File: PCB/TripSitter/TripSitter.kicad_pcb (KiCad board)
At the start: 6 copper layers, 268.6 x 82.9 mm, 257 parts, among them IC1 MT25QL256ABA1EW9-0SIT, IC2 MT41J128M16JT-125_K, IC701 IP4220CZ6, J1 Conn_ARM_JTAG_SWD_20, J10 EFM32_PinHeader_PortE, J11 EFM32_PinHeader_PortE, J12 EFM32_PinHeader_PortE, J13 EFM32_PinHeader_PortE, J14 Conn_02x10_Counter_Clockwise, J2 DE15_Plug_HighDensity_Mountin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, J201 Conn_ARM_JTAG_SWD_20, J3 USB_B_Micro, J4 USB_B_Micro, J5 Jack-DC, J6 EFM32_PinHeader_PortE, J7 HDMI_A_1.4, J801 Conn_02x05_Odd_Even, J802 Jack-DC, J803 USB_B_Micro, SW1 SW_Push_Open, SW2 SW_DPDT_x2, SW3 SW_DIP_x05, SW801 SW_DPDT_x2, U1 XC7A100T-FGG484, U2 TPS54325_PWP_14, U201 EFM32GG11B420F2048GQ100, U202 IS62WVS2568FBLL-20NLI, U5 TPS54294PWP, U6 IS62WVS2568FBLL-20NLI, U7 TPD12S520DBT, X1 XO53 100Mhz, Y201 48MHz

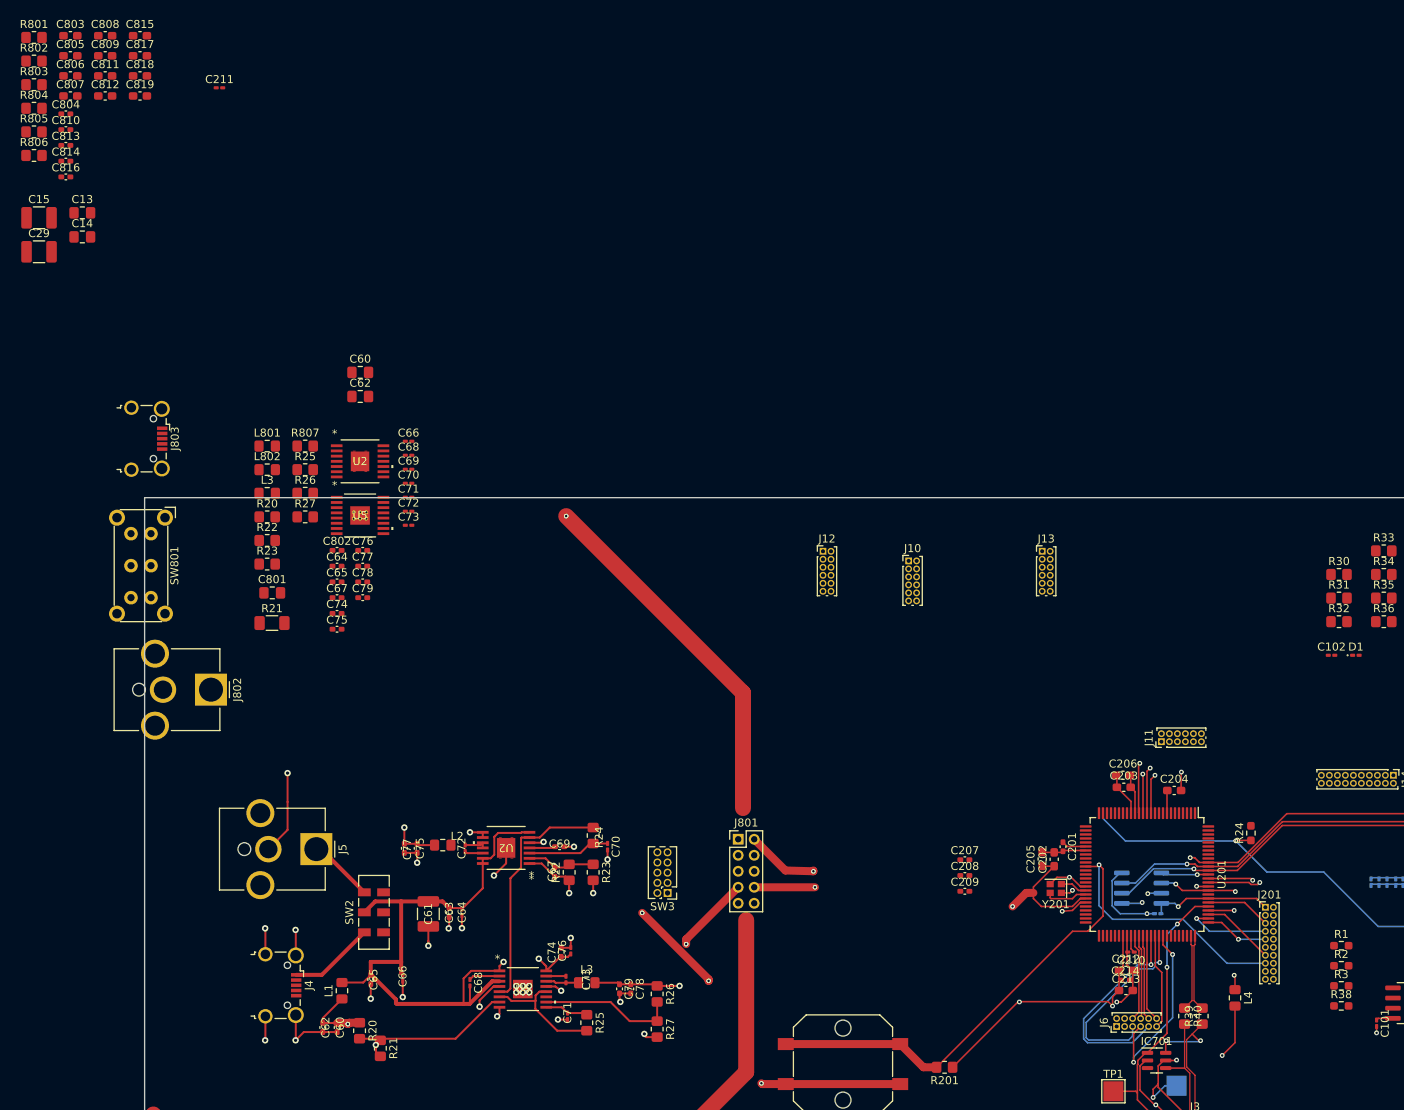
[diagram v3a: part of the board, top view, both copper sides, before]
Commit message: redo power circuit and add heat sink
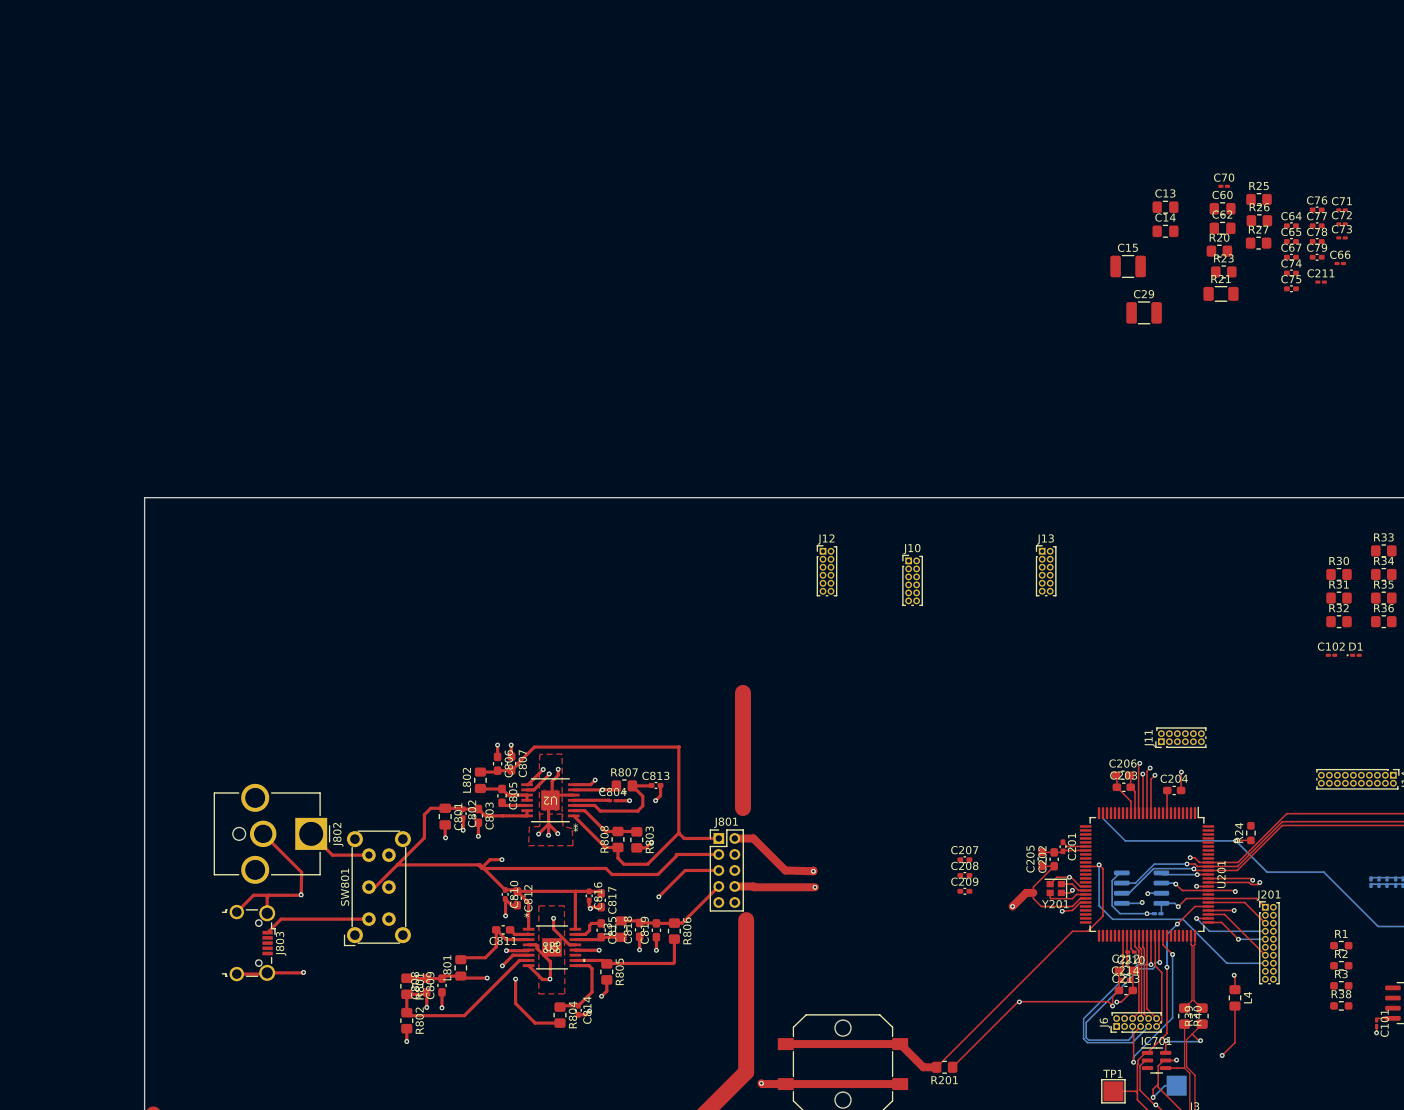
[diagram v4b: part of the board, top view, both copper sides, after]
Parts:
- removed the C60 at (39.8, 124.7)
- removed C61: 100uF, Capacitor_SMD:C_1210_3225Metric_Pad1.33x2.70mm_HandSolder
- removed the C62 at (38.0, 124.7)
- removed C63: 10uF, Capacitor_SMD:C_0402_1005Metric_Pad0.74x0.62mm_HandSolder
- removed the C64 at (55.4, 110.3)
- removed the C65 at (44.0, 118.7)
- removed the C66 at (48.0, 118.5)
- removed the C67 at (67.0, 105.3)
- removed C68: 100n, Capacitor_SMD:C_0201_0603Metric_Pad0.64x0.40mm_HandSolder
- removed C68: 100nF, Capacitor_SMD:C_0201_0603Metric_Pad0.64x0.40mm_HandSolder
- removed C69: 3.3nF, Capacitor_SMD:C_0402_1005Metric_Pad0.74x0.62mm_HandSolder
- removed the C70 at (73.6, 102.1)
- removed the C71 at (68.6, 123.3)
- removed the C72 at (55.8, 102.3)
- removed the C73 at (68.4, 118.7)
- removed the C74 at (67.8, 115.3)
- removed the C75 at (49.8, 102.3)
- removed the C76 at (69.0, 115.1)
- removed the C77 at (48.2, 102.3)
- removed the C78 at (76.5, 119.9)
- removed the C79 at (75.1, 119.9)
- removed the C804 at (5.86, 10.5)
- removed J4: USB_B_Micro, Connector_USB:USB_Micro-B_Wuerth_629105150521_CircularHoles
- removed J5: Jack-DC, Connector_BarrelJack:BarrelJack_CUI_PJ-063AH_Horizontal_CircularHoles
- removed L1, L2: 1.5uH, Inductor_SMD:L_0805_2012Metric_Pad1.15x1.40mm_HandSolder
- removed the L3 at (71.0, 119.1)
- removed the R20 at (42.6, 125.1)
- removed the R21 at (45.2, 127.3)
- removed R22: 21.3k, Resistor_SMD:R_0805_2012Metric_Pad1.20x1.40mm_HandSolder
- removed the R23 at (71.8, 105.3)
- removed the R24 at (71.8, 100.7)
- removed the R25 at (71.0, 124.1)
- removed the R26 at (79.8, 120.5)
- removed the R27 at (79.8, 124.9)
- removed SW2: SW_DPDT_x2, Button_Switch_SMD:SW_DPDT_CK_JS202011JCQN
- removed SW3: SW_DIP_x05, Connector_PinHeader_1.27mm:PinHeader_2x05_P1.27mm_Vertical
- removed the U2 at (60.9, 102.3)
- removed the U5 at (63.0, 119.9)
- R808: renamed from R22; value 21.3k -> 6.81k
- moved C211 139.8 mm to (162.8, 31.6)
- moved C29 138.3 mm to (140.6, 35.4)
- moved C15 136.3 mm to (138.6, 29.6)
- moved C13 135.4 mm to (143.3, 22.2)
- moved C14 135.4 mm to (143.3, 25.2)
- moved R804 131.0 mm to (67.6, 123.2), turned to -90 degrees
- moved R802 128.7 mm to (48.5, 123.9), turned to -90 degrees
- moved R801 127.4 mm to (48.5, 119.6), turned to -90 degrees
- moved R805 127.1 mm to (73.5, 117.8), turned to -90 degrees
- moved C76 126.7 mm to (162.3, 22.5)
- moved C64 126.7 mm to (159.1, 24.5)
- moved C65 126.7 mm to (159.1, 26.5)
- moved C67 126.7 mm to (159.1, 28.4)
- moved C74 126.7 mm to (159.1, 30.4)
- moved C75 126.7 mm to (159.1, 32.4)
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- renumbered C69 to C804
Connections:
- C811 pad 2: /PCB Power System/5V0 -> Net-(U5-SW1)
- J801 pad 10: +1V5 -> unconnected-(J801-Pin_10-Pad10)
- J801 pad 9: /PCB Power System/1V5 -> unconnected-(J801-Pin_9-Pad9)
- L801 pad 2: /PCB Power System/5V0 -> Net-(U5-SW1)
- R801 pad 2: GND -> Net-(U5-VFB1)
- R802 pad 1: GND -> Net-(U5-VFB1)
- R808 pad 1: /PCB Power System/1V5 -> /PCB Power System/1V0
- U2 pad 1: /PCB Power System/1V5 -> /PCB Power System/1V0
- U5 pad 3: /PCB Power System/5V0 -> Net-(U5-SW1)
- U5 pad 7: GND -> Net-(U5-VFB1)
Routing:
- net unconnected-(J801-Pin_10-Pad10): track 0.00 -> 137.0 mm
- net +1V5: track 163.1 -> 29.0 mm
- net /PCB Power System/1V5: track 50.1 -> 0.00 mm, vias 1 -> 0
- net /PCB Power System/1V8: track 96.3 -> 49.1 mm, vias 3 -> 2
- net /PCB Power System/1V0: track 95.8 -> 60.3 mm, vias 1 -> 0
- net /PCB Power System/3V3: track 40.1 -> 14.2 mm, vias 2 -> 0
- net GND: track 539.0 -> 518.4 mm, vias 76 -> 77
- net (no net): track 19.1 -> 0.14 mm
- net Net-(U5-EN2): track 15.5 -> 33.7 mm, vias 0 -> 3
- net Net-(U5-VFB1): track 0.00 -> 17.7 mm
- net VBUS: track 29.3 -> 42.7 mm
- net Net-(U5-SW1): track 0.00 -> 11.8 mm
- net Net-(U2-PG): track 31.2 -> 40.3 mm, vias 0 -> 2
- net Net-(SW801A-C): track 0.00 -> 8.32 mm
- net Net-(U5-VREG5): track 5.45 -> 9.95 mm
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- added copper zone on F.Cu, net GND

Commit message: pcb: Finalized routing without DDR3
Added ground and power plane, layed out all the components, fanned out
BGA. QSPI between FPGA->MCU->SRAM and MCU->SRAM is routed. Most is done
but DRC does not pass so do not produce.
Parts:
- removed C106, C107, C108, C109, C110, C111, C12, C20, C21: 4.7uF, Capacitor_SMD:C_0201_0603Metric_Pad0.64x0.40mm_HandSolder
- removed C11, C112, C113, C17, C18, C2, C22, C23, C24, C3, C4, C5, C6, C7, C8: 470nF, Capacitor_SMD:C_0201_0603Metric_Pad0.64x0.40mm_HandSolder
- removed C16, C96: 100uF, Capacitor_SMD:C_0805_2012Metric_Pad1.18x1.45mm_HandSolder
- removed C19: 47uF, Capacitor_SMD:C_0603_1608Metric_Pad1.08x0.95mm_HandSolder
- removed C207, C208: 10nF, Capacitor_SMD:C_0402_1005Metric_Pad0.74x0.62mm_HandSolder
- removed C209, C65, C67, C74: 10uF, Capacitor_SMD:C_0402_1005Metric_Pad0.74x0.62mm_HandSolder
- removed the C25 at (229.6, 125.9)
- removed the C25 at (199.6, 117.1)
- removed the C46 at (204.0, 127.8)
- removed the C46 at (204.4, 114.2)
- removed the C47 at (204.0, 128.8)
- removed the C47 at (199.4, 111.9)
- removed the C49 at (203.9, 132.1)
- removed the C49 at (209.4, 113.5)
- removed C59, C70, C71: 1uF, Capacitor_SMD:C_0201_0603Metric_Pad0.64x0.40mm_HandSolder
- removed C60, C62: 22uF, Capacitor_SMD:C_0805_2012Metric_Pad1.18x1.45mm_HandSolder
- removed C64: 0.1uF, Capacitor_SMD:C_0402_1005Metric_Pad0.74x0.62mm_HandSolder
- removed C66, C72, C73: 100nF, Capacitor_SMD:C_0201_0603Metric_Pad0.64x0.40mm_HandSolder
- removed C75, C77: 22uF, Capacitor_SMD:C_0402_1005Metric_Pad0.74x0.62mm_HandSolder
- removed C76: 100nF, Capacitor_SMD:C_0402_1005Metric_Pad0.74x0.62mm_HandSolder
- removed C78, C79: 22u, Capacitor_SMD:C_0402_1005Metric_Pad0.74x0.62mm_HandSolder
- removed C87: 47uF, Capacitor_SMD:C_1210_3225Metric_Pad1.33x2.70mm_HandSolder
- removed C88, C89: 4.7uF, Capacitor_SMD:C_0805_2012Metric_Pad1.18x1.45mm_HandSolder
- removed C94, C95: 0.1uF, Capacitor_SMD:C_0201_0603Metric_Pad0.64x0.40mm_HandSolder
- removed IC2: MT41J128M16JT-125_K, Package_BGA:Micron_FBGA-96_8x14mm_Layout9x16_P0.8mm
- removed J10, J11, J12, J13: EFM32_PinHeader_PortE, Connector_PinHeader_1.00mm:PinHeader_2x06_P1.00mm_Vertical
- removed J14: Conn_02x10_Counter_Clockwise, Connector_PinHeader_1.00mm:PinHeader_2x10_P1.00mm_Vertical
- removed R19: 100R, Resistor_SMD:R_0201_0603Metric_Pad0.64x0.40mm_HandSolder
- removed the R20 at (150.1, 27.7)
- removed the R20 at (190.3, 123.7)
- removed the R21 at (150.2, 33.0)
- removed the R21 at (191.5, 126.1)
- removed the R23 at (150.6, 30.3)
- removed the R23 at (215.8, 100.9)
- removed R25: 100k, Resistor_SMD:R_0805_2012Metric_Pad1.20x1.40mm_HandSolder
- removed R26: 73.2k, Resistor_SMD:R_0805_2012Metric_Pad1.20x1.40mm_HandSolder
- removed R27: 22.1k, Resistor_SMD:R_0805_2012Metric_Pad1.20x1.40mm_HandSolder
- removed R28: 240, Resistor_SMD:R_0805_2012Metric_Pad1.20x1.40mm_HandSolder
- removed X1: XO53 100Mhz, Oscillator:Oscillator_SMD_EuroQuartz_XO53-4Pin_5.0x3.2mm_HandSoldering
- added C25: 470nF, Capacitor_SMD:C_0402_1005Metric_Pad0.74x0.62mm_HandSolder, B.Cu at (168.7, 56.0)
- added C46: 4.7uF, Capacitor_SMD:C_0201_0603Metric_Pad0.64x0.40mm_HandSolder, B.Cu at (158.8, 68.6)
- added C47: 4.7uF, Capacitor_SMD:C_0201_0603Metric_Pad0.64x0.40mm_HandSolder, B.Cu at (160.5, 68.5)
- added C49: 4.7uF, Capacitor_SMD:C_0201_0603Metric_Pad0.64x0.40mm_HandSolder, B.Cu at (165.3, 65.9)
- added C50: 4.7uF, Capacitor_SMD:C_0201_0603Metric_Pad0.64x0.40mm_HandSolder, B.Cu at (162.6, 68.5)
- added C51: 470nF, Capacitor_SMD:C_0201_0603Metric_Pad0.64x0.40mm_HandSolder, B.Cu at (165.3, 67.6)
- added C54: 470nF, Capacitor_SMD:C_0201_0603Metric_Pad0.64x0.40mm_HandSolder, B.Cu at (169.1, 59.9)
- added C55: 470nF, Capacitor_SMD:C_0201_0603Metric_Pad0.64x0.40mm_HandSolder, B.Cu at (170.9, 62.5)
- added C56: 470nF, Capacitor_SMD:C_0201_0603Metric_Pad0.64x0.40mm_HandSolder, B.Cu at (169.7, 61.2)
- added C58: 470nF, Capacitor_SMD:C_0201_0603Metric_Pad0.64x0.40mm_HandSolder, B.Cu at (168.0, 63.9)
- added C69: 3.3nF, Capacitor_SMD:C_0201_0603Metric_Pad0.64x0.40mm_HandSolder, F.Cu at (58.5, 49.5)
- added C813: 1uF, Capacitor_SMD:C_0402_1005Metric_Pad0.74x0.62mm_HandSolder, F.Cu at (74.9, 51.7)
- added C816: 10uF, Capacitor_SMD:C_0402_1005Metric_Pad0.74x0.62mm_HandSolder, F.Cu at (52.3, 49.6)
- added L801: 1.5uH, Inductor_SMD:L_0805_2012Metric_Pad1.15x1.40mm_HandSolder, F.Cu at (80.9, 58.2)
- added R20: 10k, Resistor_SMD:R_0805_2012Metric_Pad1.20x1.40mm_HandSolder, F.Cu at (193.4, 52.6)
- added R21: 10k, Resistor_SMD:R_0805_2012Metric_Pad1.20x1.40mm_HandSolder, F.Cu at (193.4, 59.7)
- added R22: 21.3k, Resistor_SMD:R_0805_2012Metric_Pad1.20x1.40mm_HandSolder, F.Cu at (69.4, 54.3)
- added R23: 4.7k, Resistor_SMD:R_0603_1608Metric_Pad0.98x0.95mm_HandSolder, F.Cu at (187.4, 61.3)
- added U4: DSC1001DL5-100.0000T, Footprints:CDFN4_2P5X2_MCH-L, F.Cu at (189.0, 50.7)
- C1: value 330uF -> 0.1uF; footprint Capacitor_Tantalum_SMD:CP_EIA-7343-43_Kemet-X_Pad2.25x2.55mm_HandSolder -> Capacitor_SMD:C_0603_1608Metric_Pad1.08x0.95mm_HandSolder; moved to F.Cu
- C101, C102, C103, C214, C36, C37, C38, C98, D1, IC1, R1, R35, R36, R37, R38: moved to B.Cu
- C104, TP4: moved to F.Cu
- C13, C14, C26, C27: value 4.7uF -> 470nF; footprint Capacitor_SMD:C_0805_2012Metric_Pad1.18x1.45mm_HandSolder -> Capacitor_SMD:C_0402_1005Metric_Pad0.74x0.62mm_HandSolder; moved to B.Cu
- C15: value 47uF -> 470nF; footprint Capacitor_SMD:C_1210_3225Metric_Pad1.33x2.70mm_HandSolder -> Capacitor_SMD:C_0402_1005Metric_Pad0.74x0.62mm_HandSolder; moved to B.Cu
- C202, C203, C205: footprint Capacitor_SMD:C_0603_1608Metric_Pad1.08x0.95mm_HandSolder -> Capacitor_SMD:C_0402_1005Metric_Pad0.74x0.62mm_HandSolder
- C204, C206, C212, C213: footprint Capacitor_SMD:C_0603_1608Metric_Pad1.08x0.95mm_HandSolder -> Capacitor_SMD:C_0402_1005Metric_Pad0.74x0.62mm_HandSolder; moved to B.Cu
- C210: footprint Capacitor_SMD:C_0201_0603Metric_Pad0.64x0.40mm_HandSolder -> Capacitor_SMD:C_0402_1005Metric_Pad0.74x0.62mm_HandSolder; moved to B.Cu
- C28, C31: value 470nF -> 4.7uF; footprint Capacitor_SMD:C_0201_0603Metric_Pad0.64x0.40mm_HandSolder -> Capacitor_SMD:C_0402_1005Metric_Pad0.74x0.62mm_HandSolder
- C29: value 100uF -> 4.7uF; footprint Capacitor_SMD:C_1210_3225Metric_Pad1.33x2.70mm_HandSolder -> Capacitor_SMD:C_0402_1005Metric_Pad0.74x0.62mm_HandSolder; moved to B.Cu
- C30: footprint Capacitor_SMD:C_0201_0603Metric_Pad0.64x0.40mm_HandSolder -> Capacitor_SMD:C_0402_1005Metric_Pad0.74x0.62mm_HandSolder
- C32: value 470nF -> 47uF; footprint Capacitor_SMD:C_0201_0603Metric_Pad0.64x0.40mm_HandSolder -> Capacitor_SMD:C_0603_1608Metric_Pad1.08x0.95mm_HandSolder
- C33: value 4.7uF -> 100uF
- C34: value 4.7uF -> 330uF; footprint Capacitor_SMD:C_0805_2012Metric_Pad1.18x1.45mm_HandSolder -> Capacitor_Tantalum_SMD:CP_EIA-7343-43_Kemet-X_Pad2.25x2.55mm_HandSolder; moved to B.Cu
- C35: value 47uF -> 4.7uF; footprint Capacitor_SMD:C_1210_3225Metric_Pad1.33x2.70mm_HandSolder -> Capacitor_SMD:C_0201_0603Metric_Pad0.64x0.40mm_HandSolder; moved to B.Cu
- C48: value 470nF -> 4.7uF
- C52, C53, C57: value 0.1uF -> 470nF; moved to B.Cu
- C804: value 3.3nF -> 10uF; footprint Capacitor_SMD:C_0201_0603Metric_Pad0.64x0.40mm_HandSolder -> Capacitor_SMD:C_0402_1005Metric_Pad0.74x0.62mm_HandSolder
- J1: footprint Connector_PinHeader_1.00mm:PinHeader_2x10_P1.00mm_Vertical -> Connector_PinHeader_2.54mm:PinHeader_2x07_P2.54mm_Vertical_SMD
- J201: footprint Connector_PinHeader_1.00mm:PinHeader_2x10_P1.00mm_Vertical -> Connector_PinHeader_1.27mm:PinHeader_2x10_P1.27mm_Vertical_SMD
- R30: footprint Resistor_SMD:R_0805_2012Metric_Pad1.20x1.40mm_HandSolder -> Resistor_SMD:R_0603_1608Metric_Pad0.98x0.95mm_HandSolder
- R31, R32: footprint Resistor_SMD:R_0805_2012Metric_Pad1.20x1.40mm_HandSolder -> Resistor_SMD:R_0603_1608Metric_Pad0.98x0.95mm_HandSolder; moved to B.Cu
- SW1: footprint Button_Switch_SMD:SW_Push_1P1T_NO_CK_PTS125Sx43PSMTR -> Button_Switch_SMD:SW_Push_SPST_NO_Alps_SKRK
- SW801: footprint Button_Switch_THT:SW_E-Switch_EG2219_DPDT_Angled -> Button_Switch_THT:SW_E-Switch_EG1224_SPDT_Angled
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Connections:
- C1 pad 2: +1V0 -> +3.3V
- C13 pad 1: +1V5 -> +1V8
- C14 pad 1: +1V5 -> +1V8
- C15 pad 1: +1V5 -> +1V8
- C26 pad 1: +1V5 -> +1V8
- C27 pad 1: +1V5 -> +1V0
- C28 pad 1: +3.3V -> +1V8
- C29 pad 1: +1V5 -> +1V8
- C30 pad 1: +3.3V -> +1V0
- C31 pad 1: +3.3V -> +1V8
- C32 pad 1: +3.3V -> +1V8
- C33 pad 1: +3.3V -> +1V0
- C34 pad 1: +3.3V -> GND
- C34 pad 2: GND -> +1V0
- C35 pad 1: +3.3V -> +1V0
- C48 pad 1: +1V5 -> +1V0
- C52 pad 1: +3.3V -> +1V0
- C53 pad 1: +3.3V -> +1V0
- C57 pad 1: GND -> +1V0
- C57 pad 2: +3.3V -> GND
- C804 pad 1: Net-(U2-SS) -> /PCB Power System/1V5
- C804 pad 2: GND -> Net-(U2-VFB)
- C811 pad 2: Net-(U5-SW1) -> /PCB Power System/5V0
- IC701 pad 5: VBUS -> +5V
- J3 pad 1: VBUS -> +5V
- J3 pad 5: GND -> unconnected-(J3-GND-Pad5)
- J6 pad 1: /MCU EFM32GG11B420/MCU_EXTIO_PC6 -> unconnected-(J6-Pin_1-Pad1)
- J6 pad 11: /MCU EFM32GG11B420/PE_5 -> /MCU EFM32GG11B420/PE_4
- J6 pad 2: /MCU EFM32GG11B420/MCU_EXTIO_PC4 -> unconnected-(J6-Pin_2-Pad2)
- J6 pad 3: /MCU EFM32GG11B420/MCU_EXTIO_PC7 -> unconnected-(J6-Pin_3-Pad3)
- J6 pad 4: /MCU EFM32GG11B420/MCU_EXTIO_PC5 -> unconnected-(J6-Pin_4-Pad4)
- J6 pad 5: /MCU EFM32GG11B420/PE_6 -> /MCU EFM32GG11B420/PE_7
- J6 pad 7: /MCU EFM32GG11B420/PE_7 -> /MCU EFM32GG11B420/PE_6
- J6 pad 9: /MCU EFM32GG11B420/PE_4 -> /MCU EFM32GG11B420/PE_5
- J801 pad 10: unconnected-(J801-Pin_10-Pad10) -> +1V5
- J801 pad 9: unconnected-(J801-Pin_9-Pad9) -> /PCB Power System/1V5
- J802 pad 1: Net-(SW801A-C) -> Net-(SW801A-A)
- J803 pad 1: VBUS -> +5V
- L4 pad 2: VBUS -> +5V
- R24 pad 2: +3V3 -> +3.3V
- R801 pad 2: Net-(U5-VFB1) -> GND
- R802 pad 1: Net-(U5-VFB1) -> GND
- SW801 pad 1: VBUS -> Net-(SW801A-A)
- SW801 pad 3: Net-(SW801A-C) -> +5V
- TP4 pad 1: VBUS -> +5V
- U1 pad A1: (no net) -> unconnected-(U1C-IO_L1N_T0_AD4N_35-PadA1)
- U1 pad A13: unconnected-(U1B-IO_L10P_T1_16-PadA13) -> MCU_PE7
- U1 pad A14: unconnected-(U1B-IO_L10N_T1_16-PadA14) -> MCU_PE8
- U1 pad AA1: /FPGA Artix-7 100T 1FGG484C/DDR3/DDR3_DQ0 -> unconnected-(U1H-IO_L7P_T1_34-PadAA1)
- U1 pad AA10: Net-(J14-Pin_7) -> unconnected-(U1A-IO_L9P_T1_DQS_13-PadAA10)
- U1 pad AA11: Net-(J14-Pin_8) -> unconnected-(U1A-IO_L9N_T1_DQS_13-PadAA11)
- U1 pad AA17: +3.3V -> unconnected-(U1A-VCCO_13-PadAA17)
- U1 pad AA18: unconnected-(U1A-IO_L17P_T2_A14_D30_14-PadAA18) -> /FPGA Artix-7 100T 1FGG484C/VGA_B2
- U1 pad AA19: unconnected-(U1A-IO_L15P_T2_DQS_RDWR_B_14-PadAA19) -> /FPGA Artix-7 100T 1FGG484C/VGA_B1
- U1 pad AA20: /FPGA Artix-7 100T 1FGG484C/VGA_B2 -> /FPGA Artix-7 100T 1FGG484C/VGA_G3
- U1 pad AA21: /FPGA Artix-7 100T 1FGG484C/VGA_G0 -> /FPGA Artix-7 100T 1FGG484C/VGA_G1
- U1 pad AA3: /FPGA Artix-7 100T 1FGG484C/DDR3/DDR3_A8 -> unconnected-(U1H-IO_L9N_T1_DQS_34-PadAA3)
- U1 pad AA4: /FPGA Artix-7 100T 1FGG484C/DDR3/DDR3_BA2 -> unconnected-(U1H-IO_L11N_T1_SRCC_34-PadAA4)
- U1 pad AA5: /FPGA Artix-7 100T 1FGG484C/DDR3/DDR3_DQ6 -> unconnected-(U1H-IO_L10P_T1_34-PadAA5)
- U1 pad AA6: /FPGA Artix-7 100T 1FGG484C/DDR3/DDR3_A12 -> unconnected-(U1H-IO_L18N_T2_34-PadAA6)
- U1 pad AA7: +1V5 -> unconnected-(U1H-VCCO_34-PadAA7)
- U1 pad AA8: /FPGA Artix-7 100T 1FGG484C/DDR3/DDR3_UDQS_P -> unconnected-(U1H-IO_L22P_T3_34-PadAA8)
- U1 pad AA9: Net-(J14-Pin_5) -> unconnected-(U1A-IO_L8P_T1_13-PadAA9)
- U1 pad AB1: /FPGA Artix-7 100T 1FGG484C/DDR3/DDR3_LDQS_P -> unconnected-(U1H-IO_L7N_T1_34-PadAB1)
- U1 pad AB10: Net-(J14-Pin_6) -> unconnected-(U1A-IO_L8N_T1_13-PadAB10)
- U1 pad AB11: Net-(J14-Pin_3) -> unconnected-(U1A-IO_L7P_T1_13-PadAB11)
- U1 pad AB12: Net-(J14-Pin_4) -> unconnected-(U1A-IO_L7N_T1_13-PadAB12)
- U1 pad AB14: +3.3V -> unconnected-(U1A-VCCO_13-PadAB14)
- U1 pad AB18: unconnected-(U1A-IO_L17N_T2_A13_D29_14-PadAB18) -> /FPGA Artix-7 100T 1FGG484C/VGA_B3
- U1 pad AB2: /FPGA Artix-7 100T 1FGG484C/DDR3/DDR3_LDQS_N -> unconnected-(U1H-IO_L8N_T1_34-PadAB2)
- U1 pad AB20: /FPGA Artix-7 100T 1FGG484C/VGA_B3 -> /FPGA Artix-7 100T 1FGG484C/VGA_B0
- U1 pad AB21: /FPGA Artix-7 100T 1FGG484C/VGA_B1 -> /FPGA Artix-7 100T 1FGG484C/VGA_G2
- U1 pad AB22: /FPGA Artix-7 100T 1FGG484C/VGA_B0 -> /FPGA Artix-7 100T 1FGG484C/VGA_G0
- U1 pad AB3: /FPGA Artix-7 100T 1FGG484C/DDR3/DDR3_DQ4 -> unconnected-(U1H-IO_L8P_T1_34-PadAB3)
- U1 pad AB4: +1V5 -> unconnected-(U1H-VCCO_34-PadAB4)
- U1 pad AB5: /FPGA Artix-7 100T 1FGG484C/DDR3/DDR3_DQ1 -> unconnected-(U1H-IO_L10N_T1_34-PadAB5)
- U1 pad AB6: /FPGA Artix-7 100T 1FGG484C/DDR3/DDR3_LDM -> unconnected-(U1H-IO_L20N_T3_34-PadAB6)
- U1 pad AB7: /FPGA Artix-7 100T 1FGG484C/DDR3/DDR3_DQ8 -> unconnected-(U1H-IO_L20P_T3_34-PadAB7)
- U1 pad AB8: /FPGA Artix-7 100T 1FGG484C/DDR3/DDR3_DQ12 -> unconnected-(U1H-IO_L22N_T3_34-PadAB8)
- U1 pad B1: (no net) -> unconnected-(U1C-IO_L1P_T0_AD4P_35-PadB1)
- U1 pad B2: (no net) -> unconnected-(U1C-IO_L2N_T0_AD12N_35-PadB2)
- U1 pad C1: (no net) -> unconnected-(U1C-VCCO_35-PadC1)
- U1 pad C15: unconnected-(U1B-IO_L3N_T0_DQS_16-PadC15) -> MCU_PE8
- U1 pad C19: unconnected-(U1B-IO_L13N_T2_MRCC_16-PadC19) -> /FPGA Artix-7 100T 1FGG484C/SRAM_QSPI0_CS0
- U1 pad C2: (no net) -> unconnected-(U1C-IO_L2P_T0_AD12P_35-PadC2)
- U1 pad D1: (no net) -> unconnected-(U1C-IO_L3N_T0_DQS_AD5N_35-PadD1)
- U1 pad D14: /MCU EFM32GG11B420/QSPI0_SCLK -> /FPGA Artix-7 100T 1FGG484C/SRAM_QSPI0_SCLK
- U1 pad D2: (no net) -> unconnected-(U1C-IO_L4N_T0_35-PadD2)
- U1 pad E1: (no net) -> unconnected-(U1C-IO_L3P_T0_DQS_AD5P_35-PadE1)
- U1 pad E12: +1V0 -> GND
- U1 pad E2: (no net) -> unconnected-(U1C-IO_L4P_T0_35-PadE2)
- U1 pad E3: (no net) -> unconnected-(U1C-IO_L6N_T0_VREF_35-PadE3)
- U1 pad F1: (no net) -> unconnected-(U1C-IO_L5N_T0_AD13N_35-PadF1)
- U1 pad F16: unconnected-(U1B-IO_L2P_T0_16-PadF16) -> MCU_PE9
- U1 pad F2: (no net) -> unconnected-(U1C-VCCO_35-PadF2)
- U1 pad F3: (no net) -> unconnected-(U1C-IO_L6P_T0_35-PadF3)
- U1 pad F4: (no net) -> unconnected-(U1C-IO_0_35-PadF4)
- U1 pad G1: (no net) -> unconnected-(U1C-IO_L5P_T0_AD13P_35-PadG1)
- U1 pad G2: (no net) -> unconnected-(U1C-IO_L8N_T1_AD14N_35-PadG2)
- U1 pad G21: HDMI_CLK_P -> HDMI_CLK_N
- U1 pad G22: HDMI_CLK_N -> HDMI_CLK_P
- U1 pad G3: (no net) -> unconnected-(U1C-IO_L11N_T1_SRCC_35-PadG3)
- U1 pad G4: (no net) -> unconnected-(U1C-IO_L12N_T1_MRCC_35-PadG4)
- U1 pad H10: +1V8 -> +1V0
- U1 pad H12: +1V0 -> +1V8
- U1 pad H2: (no net) -> unconnected-(U1C-IO_L8P_T1_AD14P_35-PadH2)
- U1 pad H3: (no net) -> unconnected-(U1C-IO_L11P_T1_SRCC_35-PadH3)
- U1 pad H4: (no net) -> unconnected-(U1C-IO_L12P_T1_MRCC_35-PadH4)
- U1 pad H5: (no net) -> unconnected-(U1C-IO_L10N_T1_AD15N_35-PadH5)
- U1 pad H6: (no net) -> unconnected-(U1C-VCCO_35-PadH6)
- U1 pad H8: +1V8 -> +1V0
- U1 pad J1: (no net) -> unconnected-(U1C-IO_L7N_T1_AD6N_35-PadJ1)
- U1 pad J2: (no net) -> unconnected-(U1C-IO_L9N_T1_DQS_AD7N_35-PadJ2)
- U1 pad J3: (no net) -> unconnected-(U1C-VCCO_35-PadJ3)
- U1 pad J4: (no net) -> unconnected-(U1C-IO_L13N_T2_MRCC_35-PadJ4)
- U1 pad J5: (no net) -> unconnected-(U1C-IO_L10P_T1_AD15P_35-PadJ5)
- U1 pad J6: (no net) -> unconnected-(U1C-IO_L17N_T2_35-PadJ6)
- U1 pad J7: +1V8 -> +1V0
- U1 pad J9: +1V8 -> +1V0
- U1 pad K1: (no net) -> unconnected-(U1C-IO_L7P_T1_AD6P_35-PadK1)
- U1 pad K10: +1V0 -> +1V8
- U1 pad K12: +1V0 -> +1V8
- U1 pad K2: (no net) -> unconnected-(U1C-IO_L9P_T1_DQS_AD7P_35-PadK2)
- U1 pad K3: (no net) -> unconnected-(U1C-IO_L14N_T2_SRCC_35-PadK3)
- U1 pad K4: (no net) -> unconnected-(U1C-IO_L13P_T2_MRCC_35-PadK4)
- U1 pad K6: (no net) -> unconnected-(U1C-IO_L17P_T2_35-PadK6)
- U1 pad K8: +1V8 -> +1V0
- U1 pad K9: +1V0 -> GND
- U1 pad L1: (no net) -> unconnected-(U1C-IO_L15N_T2_DQS_35-PadL1)
- U1 pad L3: (no net) -> unconnected-(U1C-IO_L14P_T2_SRCC_35-PadL3)
- U1 pad L4: (no net) -> unconnected-(U1C-IO_L18N_T2_35-PadL4)
- U1 pad L5: (no net) -> unconnected-(U1C-IO_L18P_T2_35-PadL5)
- U1 pad L6: (no net) -> unconnected-(U1C-IO_25_35-PadL6)
- U1 pad L7: +1V8 -> +1V0
- U1 pad L9: unconnected-(U1F-VREFN_0-PadL9) -> GND
- U1 pad M1: (no net) -> unconnected-(U1C-IO_L15P_T2_DQS_35-PadM1)
- U1 pad M10: unconnected-(U1F-VREFP_0-PadM10) -> GND
- U1 pad M12: +1V0 -> +1V8
- U1 pad M2: (no net) -> unconnected-(U1C-IO_L16N_T2_35-PadM2)
- U1 pad M3: (no net) -> unconnected-(U1C-IO_L16P_T2_35-PadM3)
- U1 pad M4: (no net) -> unconnected-(U1C-VCCO_35-PadM4)
- U1 pad M5: (no net) -> unconnected-(U1C-IO_L23N_T3_35-PadM5)
- U1 pad M6: (no net) -> unconnected-(U1C-IO_L23P_T3_35-PadM6)
- U1 pad M8: +1V8 -> +1V0
- U1 pad N1: (no net) -> unconnected-(U1C-VCCO_35-PadN1)
- U1 pad N2: (no net) -> unconnected-(U1C-IO_L22N_T3_35-PadN2)
- U1 pad N3: (no net) -> unconnected-(U1C-IO_L19N_T3_VREF_35-PadN3)
- U1 pad N4: (no net) -> unconnected-(U1C-IO_L19P_T3_35-PadN4)
- U1 pad N5: (no net) -> unconnected-(U1C-IO_L24N_T3_35-PadN5)
- U1 pad N7: +1V8 -> +1V0
- U1 pad P1: (no net) -> unconnected-(U1C-IO_L20N_T3_35-PadP1)
- U1 pad P12: +1V0 -> +1V8
- U1 pad P2: (no net) -> unconnected-(U1C-IO_L22P_T3_35-PadP2)
- U1 pad P4: (no net) -> unconnected-(U1C-IO_L21N_T3_DQS_35-PadP4)
- U1 pad P5: (no net) -> unconnected-(U1C-IO_L21P_T3_DQS_35-PadP5)
- U1 pad P6: (no net) -> unconnected-(U1C-IO_L24P_T3_35-PadP6)
- U1 pad P8: +1V8 -> +1V0
- U1 pad R1: (no net) -> unconnected-(U1C-IO_L20P_T3_35-PadR1)
- U1 pad R11: +1V0 -> +1V8
- U1 pad R2: /FPGA Artix-7 100T 1FGG484C/DDR3/DDR3_DQ2 -> unconnected-(U1H-IO_L3N_T0_DQS_34-PadR2)
- U1 pad R3: /FPGA Artix-7 100T 1FGG484C/DDR3/DDR3_DQ7 -> unconnected-(U1H-IO_L3P_T0_DQS_34-PadR3)
- U1 pad R4: /FPGA Artix-7 100T 1FGG484C/DDR3/DDR3_CKE -> unconnected-(U1H-IO_L13P_T2_MRCC_34-PadR4)
- U1 pad R5: +1V5 -> unconnected-(U1H-VCCO_34-PadR5)
- U1 pad R6: /FPGA Artix-7 100T 1FGG484C/DDR3/DDR3_A7 -> unconnected-(U1H-IO_L17P_T2_34-PadR6)
- U1 pad T1: /FPGA Artix-7 100T 1FGG484C/DDR3/DDR3_DQ11 -> unconnected-(U1H-IO_L1P_T0_34-PadT1)
- U1 pad T14: /FPGA Artix-7 100T 1FGG484C/FPGA_BANK13_20 -> unconnected-(U1A-IO_L15P_T2_DQS_13-PadT14)
- U1 pad T15: /FPGA Artix-7 100T 1FGG484C/FPGA_BANK13_21 -> unconnected-(U1A-IO_L15N_T2_DQS_13-PadT15)
- U1 pad T16: MCU_PE9 -> unconnected-(U1A-IO_L17P_T2_13-PadT16)
- U1 pad T2: +1V5 -> unconnected-(U1H-VCCO_34-PadT2)
- U1 pad T3: /FPGA Artix-7 100T 1FGG484C/DDR3/DDR3_A10 -> unconnected-(U1H-IO_0_34-PadT3)
- U1 pad T4: /FPGA Artix-7 100T 1FGG484C/DDR3/DDR3_nWE -> unconnected-(U1H-IO_L13N_T2_MRCC_34-PadT4)
- U1 pad T5: /FPGA Artix-7 100T 1FGG484C/DDR3/DDR3_BA0 -> unconnected-(U1H-IO_L14P_T2_SRCC_34-PadT5)
- U1 pad T6: /FPGA Artix-7 100T 1FGG484C/DDR3/DDR3_ODT -> unconnected-(U1H-IO_L17N_T2_34-PadT6)
- U1 pad U1: /FPGA Artix-7 100T 1FGG484C/DDR3/DDR3_DQ9 -> unconnected-(U1H-IO_L1N_T0_34-PadU1)
- U1 pad U10: unconnected-(U1F-M1_0-PadU10) -> GND
- U1 pad U15: /FPGA Artix-7 100T 1FGG484C/FPGA_BANK13_18 -> unconnected-(U1A-IO_L14P_T2_SRCC_13-PadU15)
- U1 pad U16: MCU_PE10 -> unconnected-(U1A-IO_L17N_T2_13-PadU16)
- U1 pad U2: /FPGA Artix-7 100T 1FGG484C/DDR3/DDR3_A5 -> unconnected-(U1H-IO_L2P_T0_34-PadU2)
- U1 pad U3: /FPGA Artix-7 100T 1FGG484C/DDR3/DDR3_BA1 -> unconnected-(U1H-IO_L6P_T0_34-PadU3)
- U1 pad U5: /FPGA Artix-7 100T 1FGG484C/DDR3/DDR3_nRAS -> unconnected-(U1H-IO_L14N_T2_SRCC_34-PadU5)
- U1 pad U6: /FPGA Artix-7 100T 1FGG484C/DDR3/DDR3_nCAS -> unconnected-(U1H-IO_L16P_T2_34-PadU6)
- U1 pad U7: /FPGA Artix-7 100T 1FGG484C/DDR3/DDR3_nCS -> unconnected-(U1H-IO_25_34-PadU7)
- U1 pad U8: unconnected-(U1F-CFGBVS_0-PadU8) -> +3.3V
- U1 pad U9: unconnected-(U1F-M2_0-PadU9) -> GND
- U1 pad V10: Net-(J14-Pin_9) -> unconnected-(U1A-IO_L10P_T1_13-PadV10)
- U1 pad V13: /FPGA Artix-7 100T 1FGG484C/FPGA_BANK13_16 -> unconnected-(U1A-IO_L13P_T2_MRCC_13-PadV13)
- U1 pad V14: /FPGA Artix-7 100T 1FGG484C/FPGA_BANK13_17 -> unconnected-(U1A-IO_L13N_T2_MRCC_13-PadV14)
- U1 pad V15: /FPGA Artix-7 100T 1FGG484C/FPGA_BANK13_19 -> unconnected-(U1A-IO_L14N_T2_SRCC_13-PadV15)
- U1 pad V16: +3.3V -> unconnected-(U1A-VCCO_13-PadV16)
- U1 pad V18: /FPGA Artix-7 100T 1FGG484C/VGA_G2 -> unconnected-(U1A-IO_L14P_T2_SRCC_14-PadV18)
- U1 pad V2: /FPGA Artix-7 100T 1FGG484C/DDR3/DDR3_nRESET -> unconnected-(U1H-IO_L2N_T0_34-PadV2)
- U1 pad V3: /FPGA Artix-7 100T 1FGG484C/DDR3/XO_Enable -> unconnected-(U1H-IO_L6N_T0_VREF_34-PadV3)
- U1 pad V4: /FPGA Artix-7 100T 1FGG484C/DDR3/DDR3_A3 -> unconnected-(U1H-IO_L12P_T1_MRCC_34-PadV4)
- U1 pad V5: /FPGA Artix-7 100T 1FGG484C/DDR3/DDR3_A4 -> unconnected-(U1H-IO_L16N_T2_34-PadV5)
- U1 pad V6: +1V5 -> unconnected-(U1H-VCCO_34-PadV6)
- U1 pad V7: /FPGA Artix-7 100T 1FGG484C/DDR3/DDR3_CK_N -> unconnected-(U1H-IO_L19P_T3_34-PadV7)
- U1 pad V8: /FPGA Artix-7 100T 1FGG484C/DDR3/DDR3_CK_P -> unconnected-(U1H-IO_L21N_T3_DQS_34-PadV8)
- U1 pad V9: /FPGA Artix-7 100T 1FGG484C/DDR3/DDR3_DQ5 -> unconnected-(U1H-IO_L21P_T3_DQS_34-PadV9)
- U1 pad W1: /FPGA Artix-7 100T 1FGG484C/DDR3/DDR3_DQ15 -> unconnected-(U1H-IO_L5P_T0_34-PadW1)
- U1 pad W10: Net-(J14-Pin_10) -> unconnected-(U1A-IO_L10N_T1_13-PadW10)
- U1 pad W11: /FPGA Artix-7 100T 1FGG484C/FPGA_BANK13_15 -> unconnected-(U1A-IO_L12P_T1_MRCC_13-PadW11)
- U1 pad W12: /FPGA Artix-7 100T 1FGG484C/FPGA_BANK13_15 -> unconnected-(U1A-IO_L12N_T1_MRCC_13-PadW12)
- U1 pad W13: +3.3V -> unconnected-(U1A-VCCO_13-PadW13)
- U1 pad W14: Net-(J14-Pin_1) -> unconnected-(U1A-IO_L6P_T0_13-PadW14)
- U1 pad W15: MCU_PE7 -> unconnected-(U1A-IO_L16P_T2_13-PadW15)
- U1 pad W16: MCU_PE8 -> unconnected-(U1A-IO_L16N_T2_13-PadW16)
- U1 pad W2: /FPGA Artix-7 100T 1FGG484C/DDR3/DDR3_A9 -> unconnected-(U1H-IO_L4P_T0_34-PadW2)
- U1 pad W20: unconnected-(U1A-IO_L12N_T1_MRCC_14-PadW20) -> /FPGA Artix-7 100T 1FGG484C/GCLK100
- U1 pad W3: +1V5 -> unconnected-(U1H-VCCO_34-PadW3)
- U1 pad W4: Net-(U1H-IO_L12N_T1_MRCC_34) -> unconnected-(U1H-IO_L12N_T1_MRCC_34-PadW4)
- U1 pad W5: /FPGA Artix-7 100T 1FGG484C/DDR3/DDR3_A11 -> unconnected-(U1H-IO_L15N_T2_DQS_34-PadW5)
- U1 pad W6: /FPGA Artix-7 100T 1FGG484C/DDR3/DDR3_A0 -> unconnected-(U1H-IO_L15P_T2_DQS_34-PadW6)
- U1 pad W7: /FPGA Artix-7 100T 1FGG484C/DDR3/DDR3_DQ13 -> unconnected-(U1H-IO_L19N_T3_VREF_34-PadW7)
- U1 pad W9: /FPGA Artix-7 100T 1FGG484C/DDR3/DDR3_DQ3 -> unconnected-(U1H-IO_L24P_T3_34-PadW9)
- U1 pad Y1: /FPGA Artix-7 100T 1FGG484C/DDR3/DDR3_UDM -> unconnected-(U1H-IO_L5N_T0_34-PadY1)
- U1 pad Y10: +3.3V -> unconnected-(U1A-VCCO_13-PadY10)
- U1 pad Y11: /FPGA Artix-7 100T 1FGG484C/FPGA_BANK13_13 -> unconnected-(U1A-IO_L11P_T1_SRCC_13-PadY11)
- U1 pad Y12: /FPGA Artix-7 100T 1FGG484C/FPGA_BANK13_14 -> unconnected-(U1A-IO_L11N_T1_SRCC_13-PadY12)
- U1 pad Y14: Net-(J14-Pin_2) -> unconnected-(U1A-IO_L6N_T0_VREF_13-PadY14)
- U1 pad Y18: /FPGA Artix-7 100T 1FGG484C/VGA_G3 -> unconnected-(U1A-IO_L13P_T2_MRCC_14-PadY18)
- U1 pad Y2: /FPGA Artix-7 100T 1FGG484C/DDR3/DDR3_A13 -> unconnected-(U1H-IO_L4N_T0_34-PadY2)
- U1 pad Y3: /FPGA Artix-7 100T 1FGG484C/DDR3/DDR3_A6 -> unconnected-(U1H-IO_L9P_T1_DQS_34-PadY3)
- U1 pad Y4: /FPGA Artix-7 100T 1FGG484C/DDR3/DDR3_A2 -> unconnected-(U1H-IO_L11P_T1_SRCC_34-PadY4)
- U1 pad Y6: /FPGA Artix-7 100T 1FGG484C/DDR3/DDR3_A1 -> unconnected-(U1H-IO_L18P_T2_34-PadY6)
- U1 pad Y7: /FPGA Artix-7 100T 1FGG484C/DDR3/DDR3_UDQS_N -> unconnected-(U1H-IO_L23N_T3_34-PadY7)
- U1 pad Y8: /FPGA Artix-7 100T 1FGG484C/DDR3/DDR3_DQ14 -> unconnected-(U1H-IO_L23P_T3_34-PadY8)
- U1 pad Y9: /FPGA Artix-7 100T 1FGG484C/DDR3/DDR3_DQ10 -> unconnected-(U1H-IO_L24N_T3_34-PadY9)
- U2 pad 1: /PCB Power System/1V0 -> /PCB Power System/1V5
- U201 pad 1: Net-(J11-Pin_2) -> unconnected-(U201A-PA0-Pad1)
- U201 pad 10: /MCU EFM32GG11B420/PB1 -> unconnected-(U201A-PB1-Pad10)
- U201 pad 100: /MCU EFM32GG11B420/EBI_AD9 -> unconnected-(U201A-PA15-Pad100)
- U201 pad 11: /MCU EFM32GG11B420/PB2 -> unconnected-(U201A-PB2-Pad11)
- U201 pad 18: /MCU EFM32GG11B420/PC0 -> unconnected-(U201B-PC0-Pad18)
- U201 pad 19: /MCU EFM32GG11B420/PC1 -> unconnected-(U201B-PC1-Pad19)
- U201 pad 2: Net-(J11-Pin_4) -> unconnected-(U201A-PA1-Pad2)
- U201 pad 20: /MCU EFM32GG11B420/PC2 -> unconnected-(U201B-PC2-Pad20)
- U201 pad 21: /MCU EFM32GG11B420/PC3 -> unconnected-(U201B-PC3-Pad21)
- U201 pad 22: /MCU EFM32GG11B420/MCU_EXTIO_PC4 -> unconnected-(U201B-PC4-Pad22)
- U201 pad 23: /MCU EFM32GG11B420/MCU_EXTIO_PC5 -> unconnected-(U201B-PC5-Pad23)
- U201 pad 26: /MCU EFM32GG11B420/PA7 -> unconnected-(U201A-PA7-Pad26)
- U201 pad 27: /MCU EFM32GG11B420/PA8 -> unconnected-(U201A-PA8-Pad27)
- U201 pad 28: /MCU EFM32GG11B420/PA9 -> unconnected-(U201A-PA9-Pad28)
- U201 pad 29: /MCU EFM32GG11B420/PA10 -> unconnected-(U201A-PA10-Pad29)
- U201 pad 3: Net-(J11-Pin_6) -> unconnected-(U201A-PA2-Pad3)
- U201 pad 30: /MCU EFM32GG11B420/PA11 -> unconnected-(U201A-PA11-Pad30)
- U201 pad 33: /MCU EFM32GG11B420/EBI_AD10 -> unconnected-(U201A-PA12-Pad33)
- U201 pad 34: /MCU EFM32GG11B420/EBI_AD11 -> unconnected-(U201A-PA13-Pad34)
- U201 pad 35: /MCU EFM32GG11B420/EBI_AD12 -> unconnected-(U201A-PA14-Pad35)
- U201 pad 37: /MCU EFM32GG11B420/PB9 -> unconnected-(U201A-PB9-Pad37)
- U201 pad 38: /MCU EFM32GG11B420/PB10 -> unconnected-(U201A-PB10-Pad38)
- U201 pad 39: /MCU EFM32GG11B420/PB11 -> unconnected-(U201A-PB11-Pad39)
- U201 pad 4: Net-(J11-Pin_8) -> unconnected-(U201A-PA3-Pad4)
- U201 pad 40: /MCU EFM32GG11B420/PB12 -> unconnected-(U201A-PB12-Pad40)
- U201 pad 46: Net-(J12-Pin_1) -> unconnected-(U201B-PD0-Pad46)
- U201 pad 47: Net-(J12-Pin_3) -> unconnected-(U201B-PD1-Pad47)
- U201 pad 48: Net-(J12-Pin_5) -> unconnected-(U201B-PD2-Pad48)
- U201 pad 49: Net-(J12-Pin_7) -> unconnected-(U201B-PD3-Pad49)
- U201 pad 5: Net-(J11-Pin_10) -> unconnected-(U201A-PA4-Pad5)
- U201 pad 50: Net-(J12-Pin_9) -> unconnected-(U201B-PD4-Pad50)
- U201 pad 51: Net-(J12-Pin_11) -> unconnected-(U201B-PD5-Pad51)
- U201 pad 55: /MCU EFM32GG11B420/MCU_EXTIO_PC7 -> unconnected-(U201B-PC6-Pad55)
- U201 pad 56: /MCU EFM32GG11B420/MCU_EXTIO_PC6 -> unconnected-(U201B-PC7-Pad56)
- U201 pad 6: Net-(J11-Pin_12) -> unconnected-(U201A-PA5-Pad6)
- U201 pad 68: /MCU EFM32GG11B420/PC3 -> unconnected-(U201B-PC8-Pad68)
- U201 pad 69: /MCU EFM32GG11B420/PC9 -> unconnected-(U201B-PC9-Pad69)
- U201 pad 7: /MCU EFM32GG11B420/PA6 -> unconnected-(U201A-PA6-Pad7)
- U201 pad 70: /MCU EFM32GG11B420/PC10 -> unconnected-(U201B-PC10-Pad70)
- U201 pad 71: /MCU EFM32GG11B420/PC11 -> unconnected-(U201B-PC11-Pad71)
- U201 pad 84: /MCU EFM32GG11B420/QSPI0_SCLK -> /FPGA Artix-7 100T 1FGG484C/SRAM_QSPI0_SCLK
- U201 pad 9: /MCU EFM32GG11B420/PB0 -> unconnected-(U201A-PB0-Pad9)
- U201 pad 95: MCU_PE10 -> unconnected-(U201C-PE11-Pad95)
- U201 pad 96: /MCU EFM32GG11B420/EBI_AD4 -> unconnected-(U201C-PE12-Pad96)
- U201 pad 97: /MCU EFM32GG11B420/EBI_AD5 -> unconnected-(U201C-PE13-Pad97)
- U201 pad 98: /MCU EFM32GG11B420/EBI_AD6 -> unconnected-(U201C-PE14-Pad98)
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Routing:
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- added copper zone on In2.Cu, net +3.3V
- removed copper zone on In4.Cu, net GND
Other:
- board size 268.6 x 82.9 mm -> 203 x 85 mm
- copper layers 6 -> 4

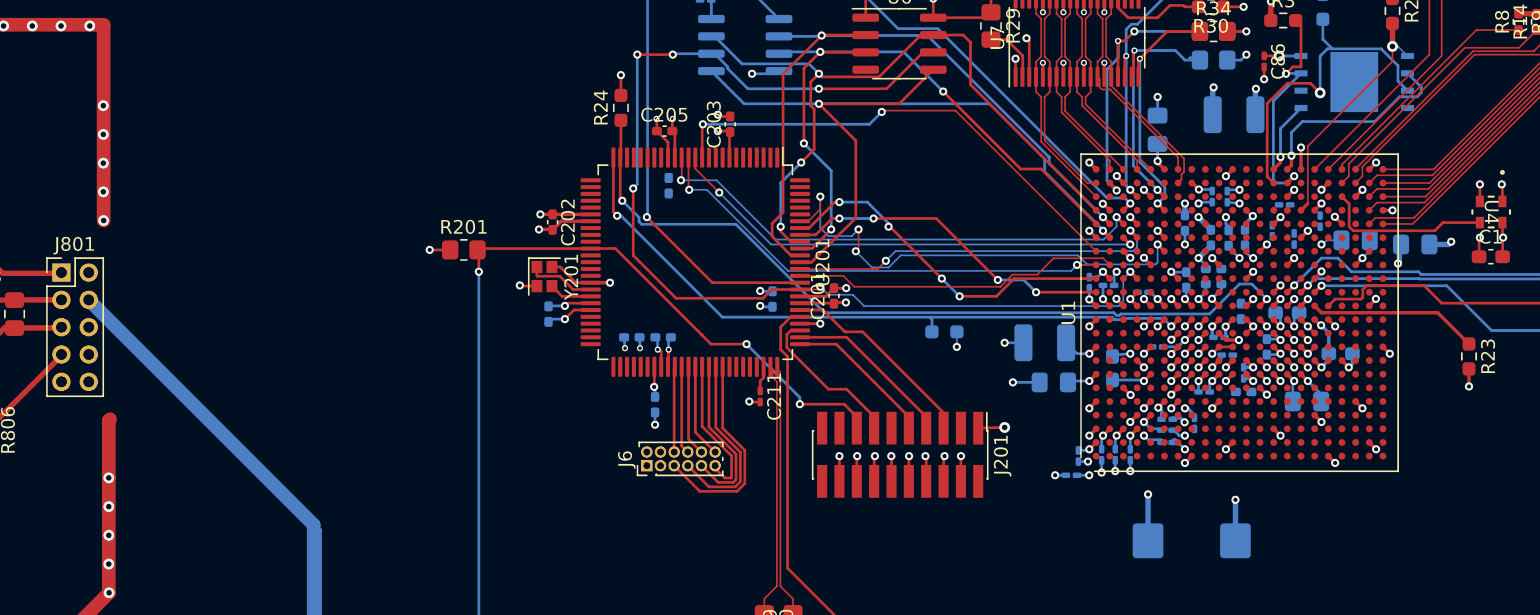
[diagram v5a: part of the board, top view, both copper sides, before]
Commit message: pcb: 3.3V voltage rails fixup and connected IC2
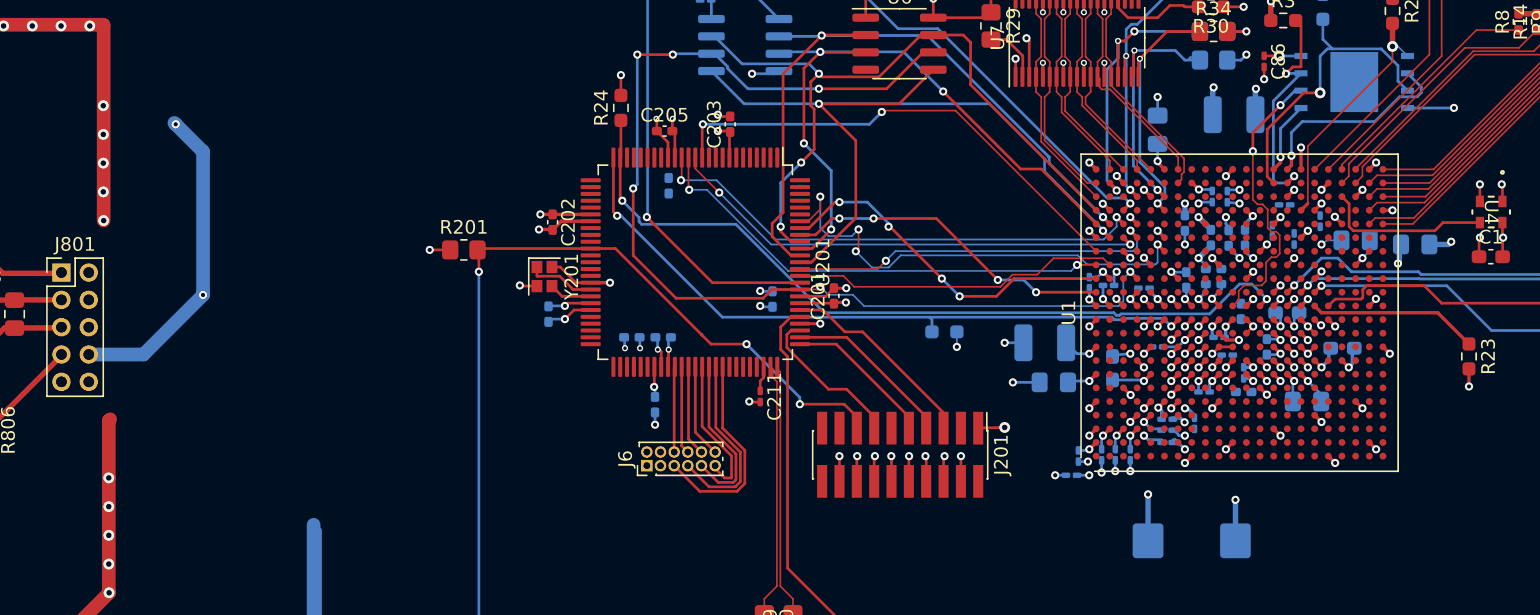
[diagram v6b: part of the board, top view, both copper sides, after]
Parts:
- moved C10 0.42 mm to (178.1, 60.7)
- moved C101 0.31 mm to (163.6, 56.3)
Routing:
- net +5V: track 269.1 -> 221.9 mm
- net +3.3V: track 100.8 -> 125.6 mm, vias 55 -> 57
- net Net-(IC1-C): track 0.00 -> 21.1 mm, vias 0 -> 2
- net GND: track 507.2 -> 511.6 mm, vias 214 -> 215
- net +1V8: track 124.2 -> 121.1 mm
- net /FPGA Artix-7 100T 1FGG484C/Programmer interface/QSPI_DQ2: track 24.5 -> 22.8 mm
